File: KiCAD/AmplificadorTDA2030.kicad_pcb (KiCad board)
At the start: 2 copper layers, 75 x 60 mm, 46 parts, among them J1 R_Speaker, J2 SJ1-3523N, J3 DC-005, J4 L_Speaker, U1 TDA2030, U2 TDA2030

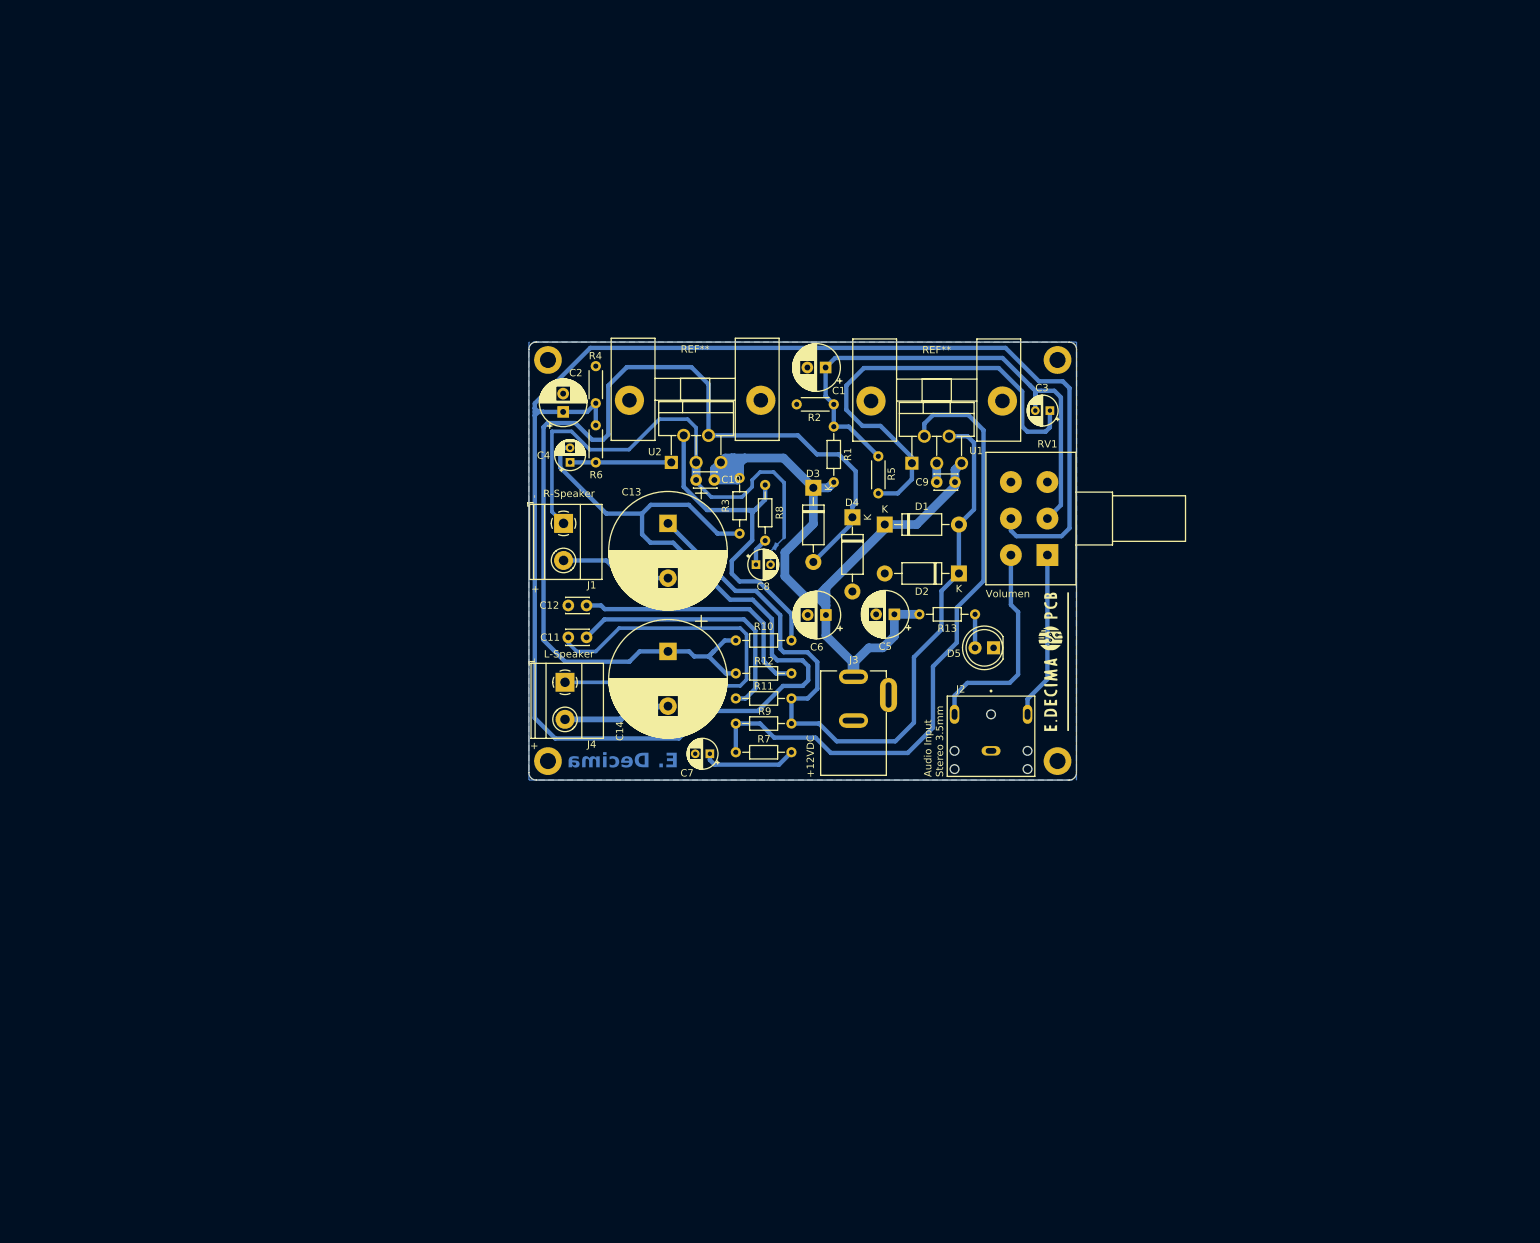
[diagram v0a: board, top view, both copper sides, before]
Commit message: Reorganizacion de Carpetas y Actualizacion de Documentacion
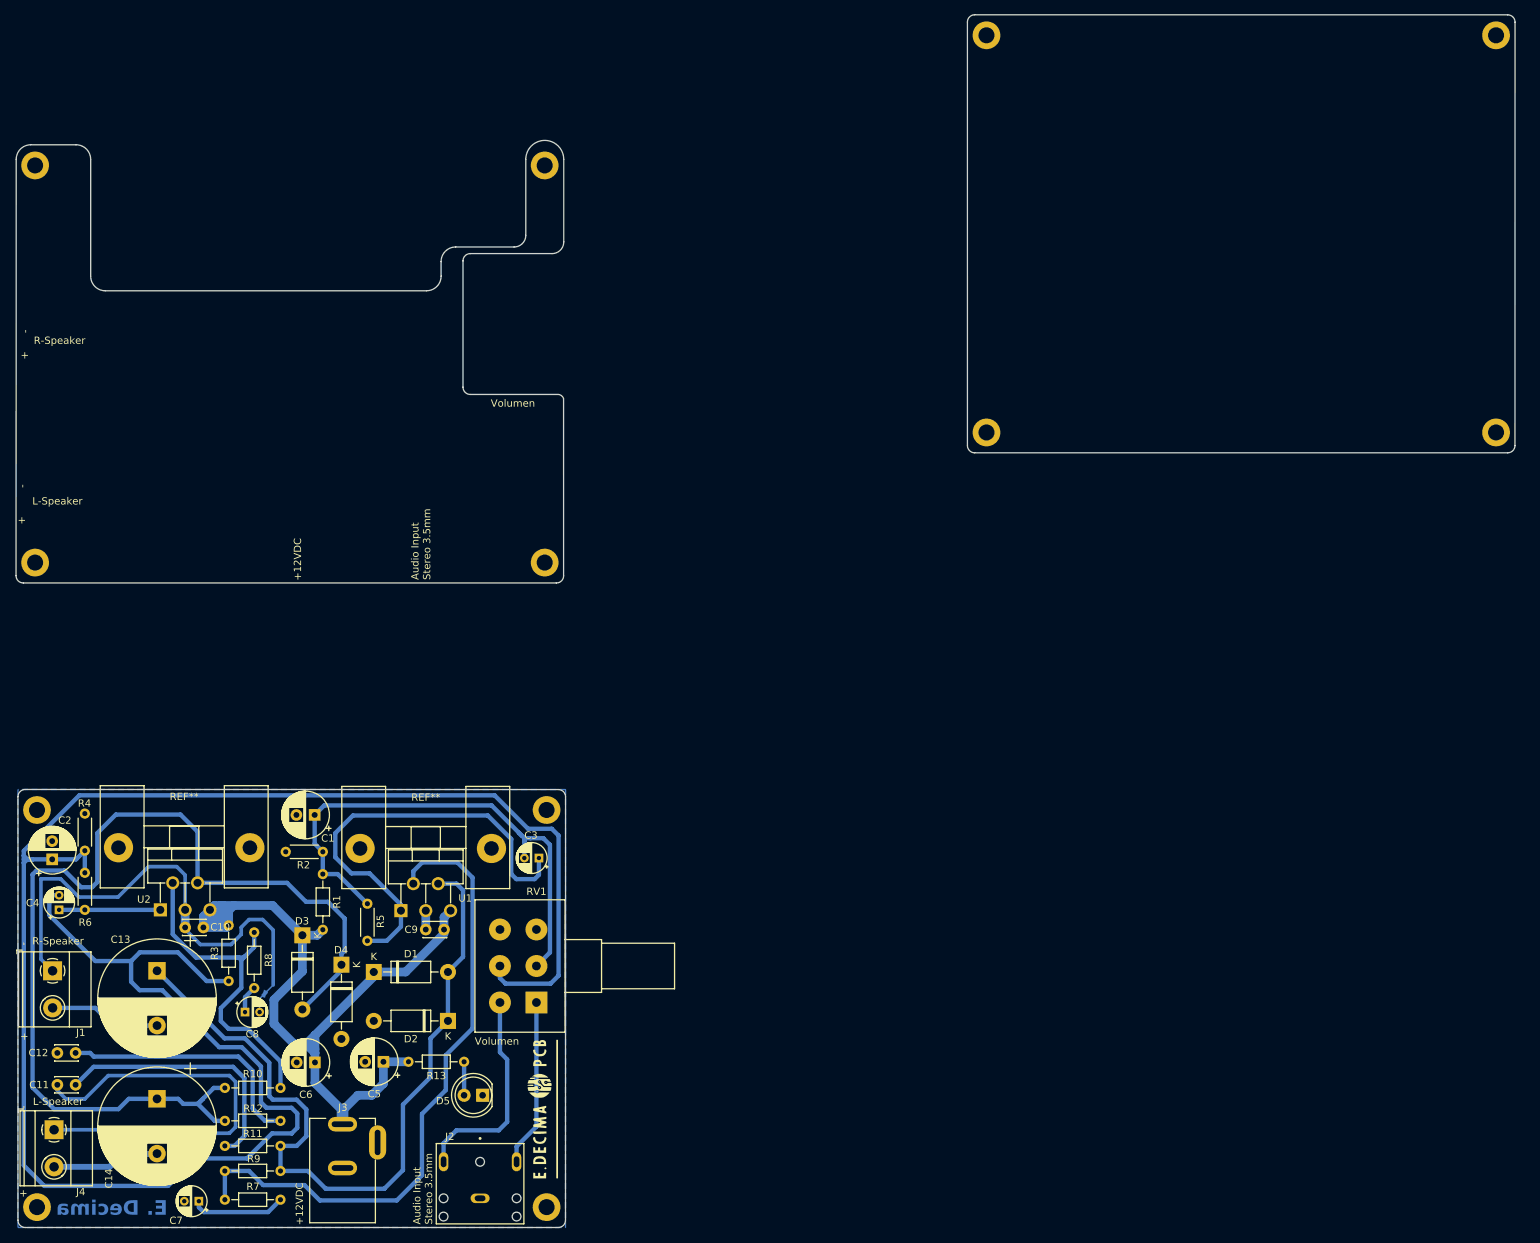
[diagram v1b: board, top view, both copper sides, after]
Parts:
- added ?: , , F.Cu at (44.8, 93.6)
- added ?: , , F.Cu at (175.1, 75.8)
- added REF**: MountingHole_2.2mm_M2_DIN965_Pad, MountingHole:MountingHole_2.2mm_M2_DIN965_Pad, F.Cu at (175.1, 21.4)
- added REF**: MountingHole_2.2mm_M2_DIN965_Pad, MountingHole:MountingHole_2.2mm_M2_DIN965_Pad, F.Cu at (244.9, 21.4)
- added REF**: MountingHole_2.2mm_M2_DIN965_Pad, MountingHole:MountingHole_2.2mm_M2_DIN965_Pad, F.Cu at (114.6, 39.2)
- added REF**: MountingHole_2.2mm_M2_DIN965_Pad, MountingHole:MountingHole_2.2mm_M2_DIN965_Pad, F.Cu at (244.9, 75.8)
- added REF**: MountingHole_2.2mm_M2_DIN965_Pad, MountingHole:MountingHole_2.2mm_M2_DIN965_Pad, F.Cu at (44.8, 39.2)
- added REF**: MountingHole_2.2mm_M2_DIN965_Pad, MountingHole:MountingHole_2.2mm_M2_DIN965_Pad, F.Cu at (114.6, 93.6)
- moved REF** 93.3 mm to (45.0, 127.5)
- moved REF** 93.3 mm to (114.8, 127.5)
- moved C7 93.0 mm to (67.2, 181.1)
- moved C10 93.0 mm to (65.3, 143.6)
- moved C2 93.0 mm to (47.1, 134.3)
- moved C9 93.0 mm to (98.3, 143.9)
- moved J1 93.0 mm to (47.2, 149.6)
- moved J2 93.0 mm to (105.7, 180.7)
- moved R1 93.0 mm to (84.2, 136.3)
- moved R10 93.0 mm to (70.8, 165.6)
- moved R2 93.0 mm to (79.1, 133.2)
- moved R4 93.0 mm to (51.6, 128.0)
- moved R5 93.0 mm to (90.3, 140.4)
- moved R6 93.0 mm to (51.6, 136.1)
- moved C1 93.0 mm to (83.1, 128.2)
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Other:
- board size 75 x 60 mm -> 205.3 x 166.1 mm

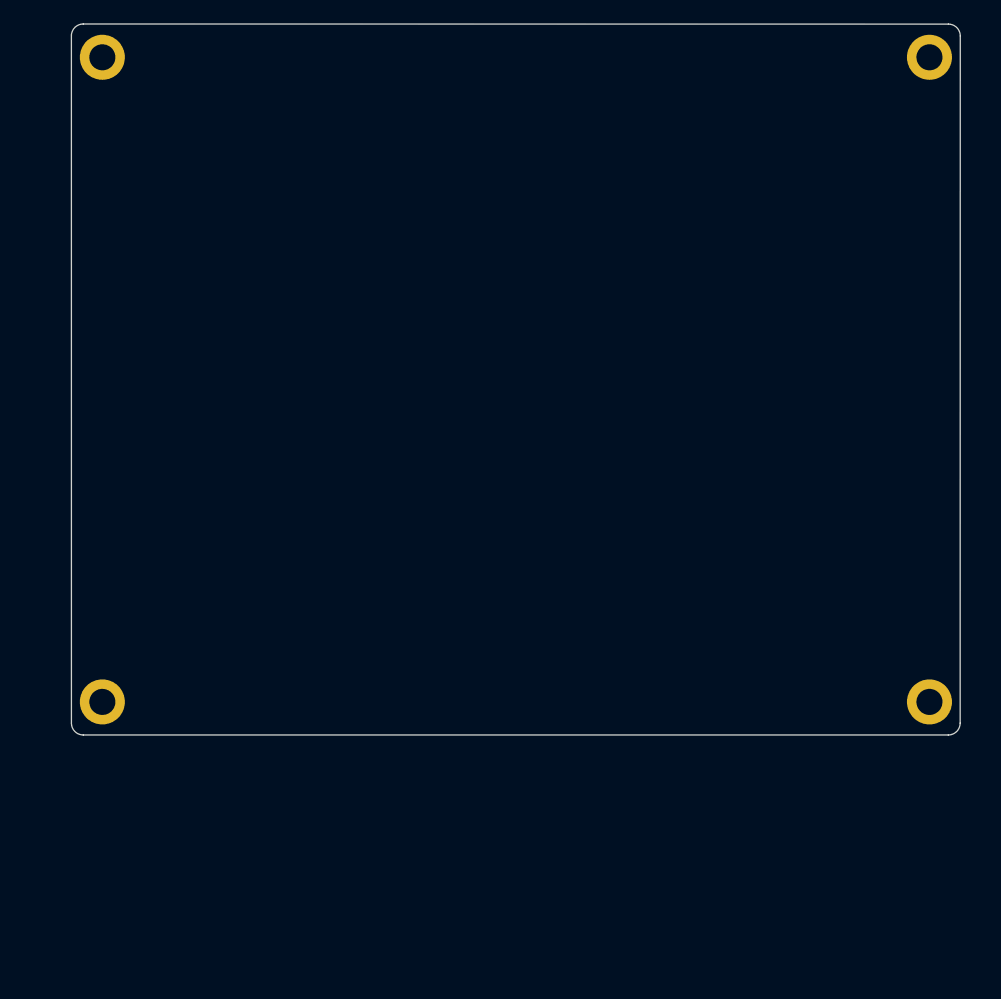
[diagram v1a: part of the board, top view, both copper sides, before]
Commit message: Agrego diseño mecanico en AutoCAD
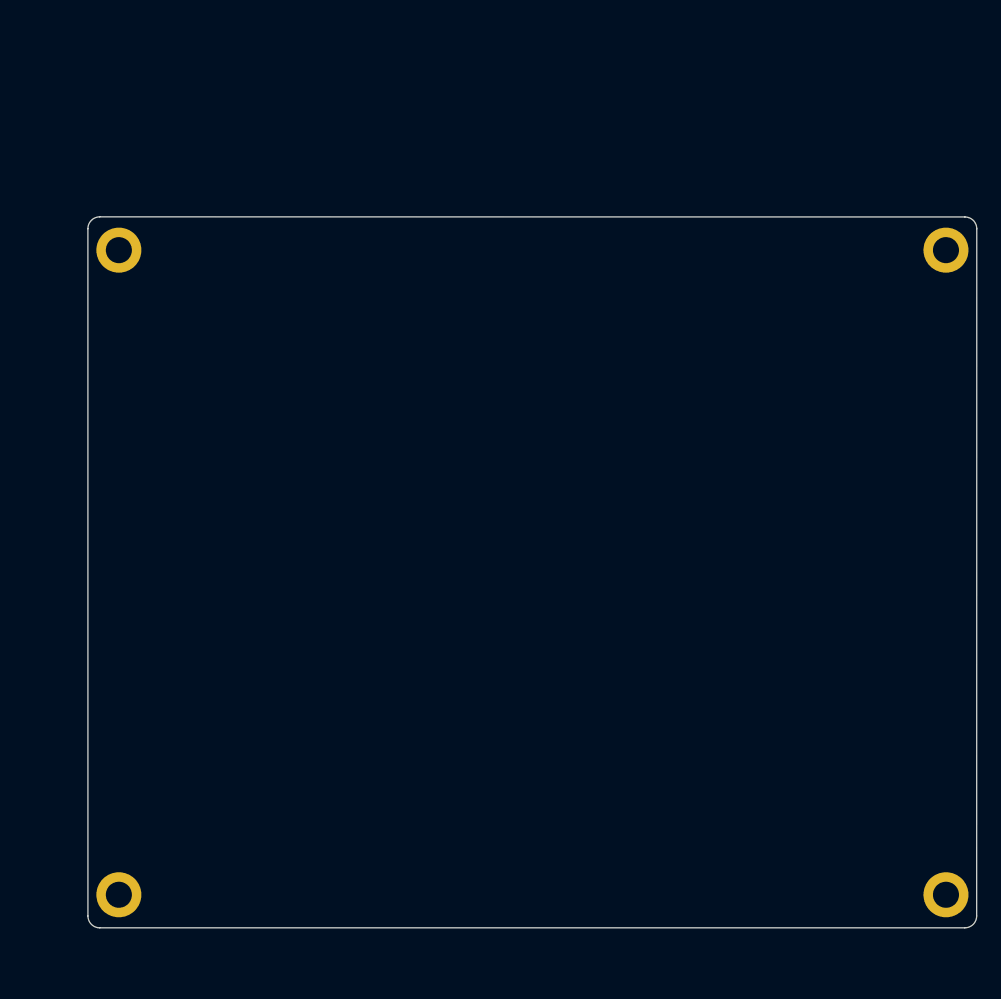
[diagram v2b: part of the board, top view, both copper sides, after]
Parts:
- moved REF** 16.3 mm to (246.3, 37.7)
- moved REF** 16.3 mm to (176.5, 37.7)
- moved REF** 16.3 mm to (246.3, 92.1)
- moved ? 16.3 mm to (176.5, 92.1)
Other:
- board size 205.3 x 166.1 mm -> 206.7 x 149.8 mm
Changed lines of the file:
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@@
 	(footprint ""
 		(layer "F.Cu")
-		(at 175.106446 75.805)
+		(at 176.5 92.08)
 		(property "Reference" ""
 			(at 0 0 0)
@@
 	(footprint "MountingHole:MountingHole_2.2mm_M2_DIN965_Pad"
 		(layer "F.Cu")
-		(at 244.906446 75.805)
+		(at 246.3 92.08)
 		(descr "Mounting Hole 2.2mm, M2, DIN965")
 		(tags "mounting hole 2.2mm m2 din965")
@@
 	(footprint "MountingHole:MountingHole_2.2mm_M2_DIN965_Pad"
 		(layer "F.Cu")
-		(at 175.106446 21.405)
+		(at 176.5 37.68)
 		(descr "Mounting Hole 2.2mm, M2, DIN965")
 		(tags "mounting hole 2.2mm m2 din965")
@@
 	(footprint "MountingHole:MountingHole_2.2mm_M2_DIN965_Pad"
 		(layer "F.Cu")
-		(at 244.906446 21.405)
+		(at 246.3 37.68)
 		(descr "Mounting Hole 2.2mm, M2, DIN965")
 		(tags "mounting hole 2.2mm m2 din965")
@@
 	)
 	(gr_line
-		(start 172.496446 77.595)
-		(end 172.493553 19.595)
+		(start 173.89 93.87)
+		(end 173.887107 35.87)
 		(stroke
 			(width 0.05)
@@
 	)
 	(gr_arc
-		(start 246.506446 18.605)
-		(mid 247.213553 18.897893)
-		(end 247.506446 19.605)
+		(start 247.9 34.88)
+		(mid 248.607077 35.172909)
+		(end 248.9 35.88)
 		(stroke
 			(width 0.05)
@@
 	)
 	(gr_line
-		(start 247.506446 19.605)
-		(end 247.496446 77.595)
+		(start 248.9 35.88)
+		(end 248.89 93.87)
 		(stroke
 			(width 0.05)
@@
 	)
 	(gr_arc
-		(start 173.496446 78.595)
-		(mid 172.789339 78.302107)
-		(end 172.496446 77.595)
+		(start 174.89 94.87)
+		(mid 174.182863 94.577123)
+		(end 173.89 93.87)
 		(stroke
 			(width 0.05)
@@
 	)
 	(gr_line
-		(start 173.493553 18.595)
-		(end 246.506446 18.605)
+		(start 174.887107 34.87)
+		(end 247.9 34.88)
 		(stroke
 			(width 0.05)
@@
 	)
 	(gr_line
-		(start 246.496446 78.595)
-		(end 173.496446 78.595)
+		(start 247.89 94.87)
+		(end 174.89 94.87)
 		(stroke
 			(width 0.05)
@@
 	)
 	(gr_arc
-		(start 172.493553 19.595)
-		(mid 172.786448 18.887895)
-		(end 173.493553 18.595)
+		(start 173.887107 35.87)
+		(mid 174.179997 35.162877)
+		(end 174.887107 34.87)
 		(stroke
 			(width 0.05)
@@
 	)
 	(gr_arc
-		(start 247.496446 77.595)
-		(mid 247.203553 78.302107)
-		(end 246.496446 78.595)
+		(start 248.89 93.87)
+		(mid 248.59711 94.577123)
+		(end 247.89 94.87)
 		(stroke
 			(width 0.05)
@@
 			(xy 117.2 38) (xy 42.2 38)
 		)
-		(height 24.8)
+		(height 20.6)
 		(gr_text "75,0000 mm"
-			(at 79.6 13.4 0)
+			(at 80.2 17.4 0)
 			(layer "User.4")
 			(effects
@@
 		(layer "User.4")
 		(pts
-			(xy 244.906446 75.805) (xy 244.906446 78.605)
+			(xy 246.3 92.08) (xy 246.3 94.88)
 		)
 		(height -7)
 		(gr_text "2,8000 mm"
-			(at 253.506446 77.005 90)
+			(at 254.9 93.28 90)
 			(layer "User.4")
 			(effects
@@
 		(layer "User.4")
 		(pts
-			(xy 245.001446 90.47) (xy 247.601446 90.47)
+			(xy 246.395 106.745) (xy 248.995 106.745)
 		)
 		(height -4.8)
 		(gr_text "2,6000 mm"
-			(at 246.301446 84.52 0)
+			(at 247.695 100.795 0)
+			(layer "User.4")
+			(effects
+				(font
+					(size 1 1)
+					(thickness 0.15)
+				)
+			)
+		)
+		(format
+			(prefix "")
+			(suffix "")
+			(units 3)
+			(units_format 1)
+			(precision 4)
+		)
+		(style
+			(thickness 0.1)
+			(arrow_length 1.27)
+			(text_position_mode 0)
+			(extension_height 0.58642)
+			(extension_offset 0.5) keep_text_aligned)
+	)
+	(dimension
+		(type aligned)
+		(layer "User.4")
+		(pts
+			(xy 108.11 50.4) (xy 108.11 51.33)
+		)
+		(height 11.99)
+		(gr_text "0,9300 mm"
+			(at 94.97 50.865 90)
 			(layer "User.4")
 			(effects
@@
 		(layer "User.4")
 		(pts
-			(xy 172.501446 18.6) (xy 172.501446 78.6)
+			(xy 173.895 34.875) (xy 173.895 94.875)
 		)
 		(height 4.789999)
 		(gr_text "60,0000 mm"
-			(at 166.561447 48.6 90)
+			(at 167.955001 64.875 90)
 			(layer "User.4")
 			(effects
@@
 		(layer "User.4")
 		(pts
-			(xy 244.906446 21.405) (xy 247.506446 21.405)
+			(xy 246.3 37.68) (xy 248.9 37.68)
 		)
 		(height -4.8)
 		(gr_text "2,6000 mm"
-			(at 246.206446 15.455 0)
+			(at 247.6 31.73 0)
 			(layer "User.4")
 			(effects
@@
 		(layer "User.4")
 		(pts
-			(xy 172.496446 78.595) (xy 247.496446 78.595)
+			(xy 173.89 94.87) (xy 248.89 94.87)
 		)
 		(height 4.01)
 		(gr_text "75,0000 mm"
-			(at 209.996446 81.455 0)
+			(at 211.39 97.73 0)
 			(layer "User.4")
 			(effects
@@
 			(extension_height 0.58642)
 			(extension_offset 0.5) keep_text_aligned)
+	)
+	(dimension
+		(type aligned)
+		(layer "User.4")
+		(pts
+			(xy 50.4 36.4) (xy 50.4 56.4)
+		)
+		(height -26)
+		(gr_text "20,0000 mm"
+			(at 76.2 46.4 90)
+			(layer "User.4")
+			(effects
+				(font
+					(size 1 1)
+					(thickness 0.15)
+				)
+			)
+		)
+		(format
+			(prefix "")
+			(suffix "")
+			(units 3)
+			(units_format 1)
+			(precision 4)
+		)
+		(style
+			(thickness 0.1)
+			(arrow_length 1.27)
+			(text_position_mode 2)
+			(extension_height 0.58642)
+			(extension_offset 0.5) keep_text_aligned)

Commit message: Archivos Imprimibles
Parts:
- removed the ? at (44.8, 93.6)
- removed the ? at (176.5, 92.1)
- removed the REF** at (176.5, 37.7)
- removed the REF** at (246.3, 37.7)
- removed the REF** at (114.6, 39.2)
- removed the REF** at (246.3, 92.1)
- removed the REF** at (44.8, 39.2)
- removed the REF** at (114.6, 93.6)
- moved C9 89.2 mm to (162.0, 81.4)
- moved J2 89.2 mm to (169.4, 118.2)
- moved R1 89.2 mm to (147.9, 73.8)
- moved R5 89.2 mm to (154.0, 77.8)
- moved ? 89.2 mm to (108.7, 119.4)
- moved C10 89.2 mm to (129.0, 81.1)
- moved C2 89.2 mm to (110.8, 71.8)
- moved C3 89.2 mm to (177.5, 71.6)
- moved C7 89.2 mm to (130.9, 118.6)
- moved G*** 89.2 mm to (177.9, 106.0)
- moved R13 89.2 mm to (167.2, 99.5)
- moved R3 89.2 mm to (135.0, 88.4)
- moved R4 89.2 mm to (115.3, 65.5)
- moved R6 89.2 mm to (115.3, 73.6)
- moved R8 89.2 mm to (138.5, 89.4)
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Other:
- board size 206.7 x 149.8 mm -> 75.8 x 60.6 mm

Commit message: Imagenes de PCB
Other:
- board text added: "G"
- board text added: "L"
- board text added: "R"
